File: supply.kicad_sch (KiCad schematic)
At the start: 72 parts, among them J301 Molex_Nano-Fit_1x2_SMD_105430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, Q301 DZDH0401DW, Q302 DZDH0401DW, Q303 DZDH0401DW, Q304 SQS401EN-T1_BE3, Q305 SQS401EN-T1_BE3, Q306 SQS401EN-T1_BE3, Q307 SQS401EN-T1_BE3, U301 AP62301WU-7, U302 AP62301WU-7, U303 AP62600SJ-7

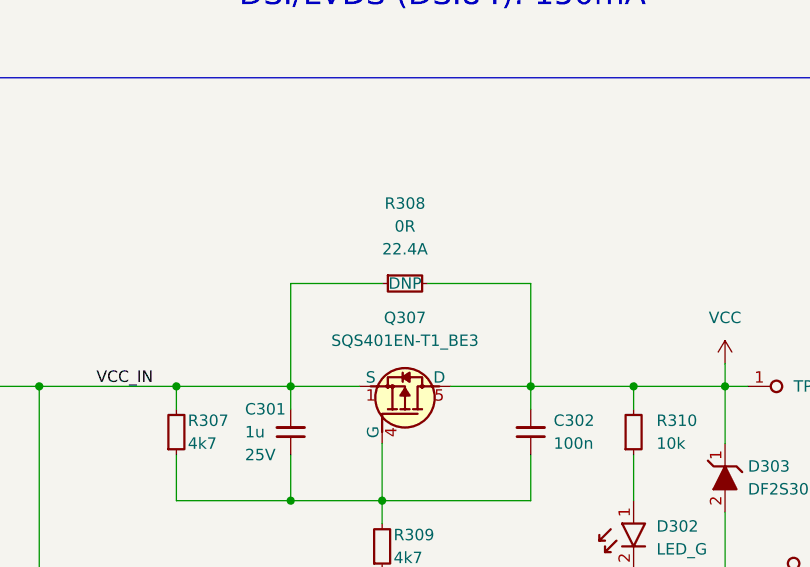
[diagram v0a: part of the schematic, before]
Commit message: Sch: Clean incorrect symbol references; Cleanup DNPs
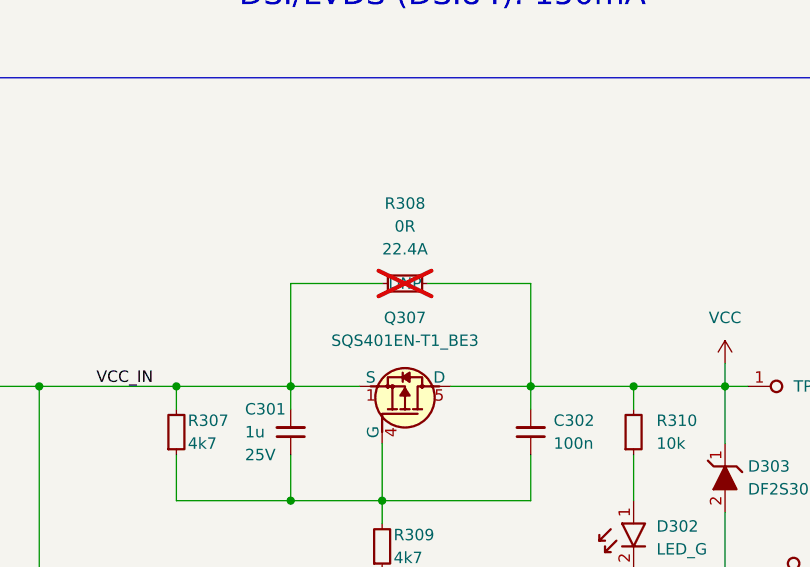
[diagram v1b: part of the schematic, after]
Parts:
- R308: now not fitted; now left out of the parts list
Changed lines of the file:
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@@
   )
   (symbol (lib_id "antmicroResistors0603:R_0R_22.4A_0603") (at 147.32 110.49 0) (unit 1)
-    (in_bom yes) (on_board yes) (dnp no)
+    (in_bom no) (on_board yes) (dnp yes)
     (property "Reference" "R308" (at 149.86 101.6 0)
       (effects (font (size 1.27 1.27)))

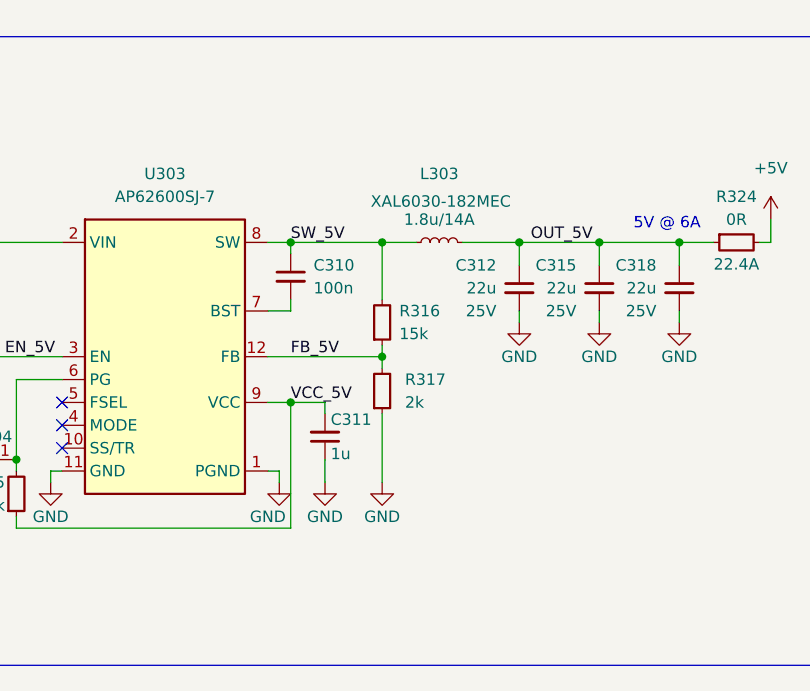
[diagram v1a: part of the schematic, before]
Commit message: [#55181] PCB: update DCDC(5V & 3V3) layout; Sch: correct 5V DCDC feedback
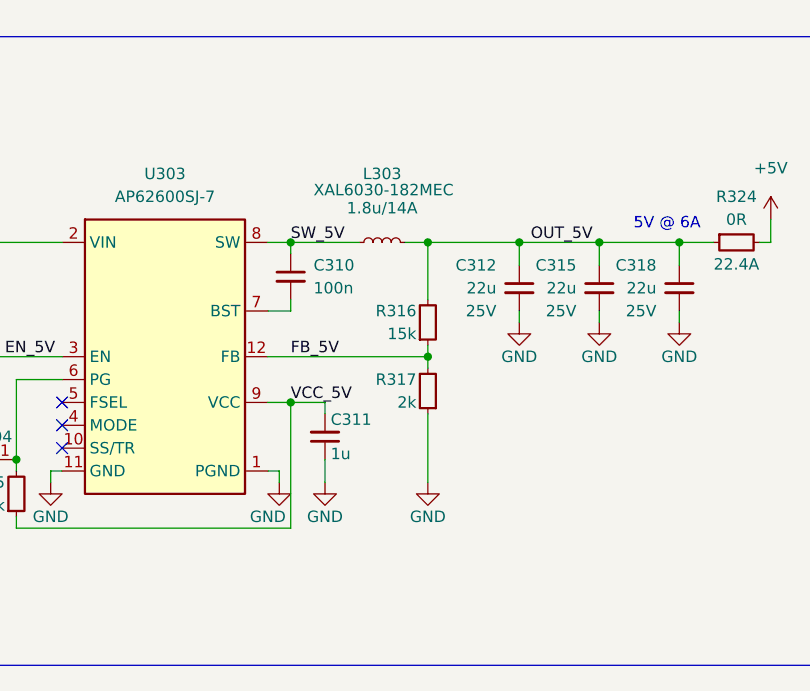
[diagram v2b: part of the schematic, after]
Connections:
- net OUT_5V: now also R316.2
- net SW_5V: no longer R316.2
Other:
- moved on the sheet: L303, R316, R317

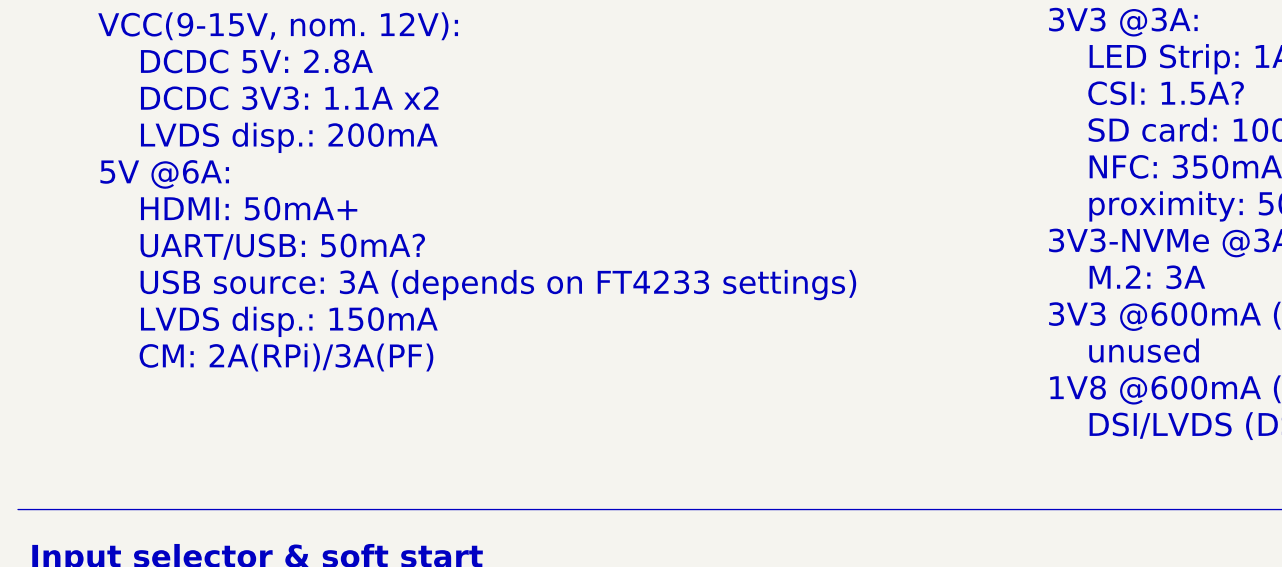
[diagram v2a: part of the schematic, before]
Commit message: [#55532] Update USB sch according to review notes; update related layout
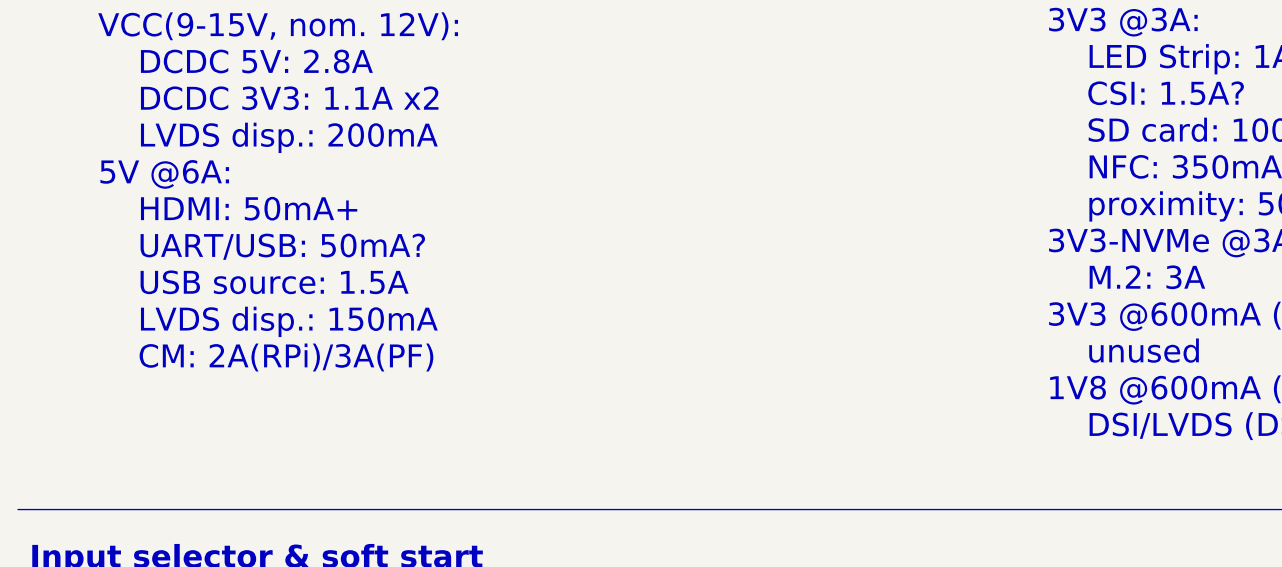
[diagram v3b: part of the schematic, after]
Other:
- note added: "VCC(9-15V, nom. 12V): DCDC 5V: 2.8A DCDC 3V3: 1.1A x2 LVDS disp.: 200mA 5V @6A: HDMI: 50mA+ UART/USB: 50mA? USB source: 1.5A LVDS disp.: 150mA CM: 2A(RPi)/3A(PF)"
- note removed: "VCC(9-15V, nom. 12V): DCDC 5V: 2.8A DCDC 3V3: 1.1A x2 LVDS disp.: 200mA 5V @6A: HDMI: 50mA+ UART/USB: 50mA? USB source: 3A (depends on FT4233 settings) LVDS disp.: 150mA CM: 2A(RPi)/3A(PF)"
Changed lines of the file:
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@@
     (effects (font (size 2.54 2.54)) (justify left bottom))
   )
-  (text "VCC(9-15V, nom. 12V):\n	DCDC 5V: 2.8A\n	DCDC 3V3: 1.1A x2\n	LVDS disp.: 200mA \n5V @6A:\n	HDMI: 50mA+\n	UART/USB: 50mA?\n	USB source: 3A (depends on FT4233 settings)\n	LVDS disp.: 150mA\n	CM: 2A(RPi)/3A(PF)\n"
+  (text "VCC(9-15V, nom. 12V):\n	DCDC 5V: 2.8A\n	DCDC 3V3: 1.1A x2\n	LVDS disp.: 200mA \n5V @6A:\n	HDMI: 50mA+\n	UART/USB: 50mA?\n	USB source: 1.5A\n	LVDS disp.: 150mA\n	CM: 2A(RPi)/3A(PF)\n"
     (at 21.59 72.39 0)
     (effects (font (size 2.54 2.54)) (justify left bottom))

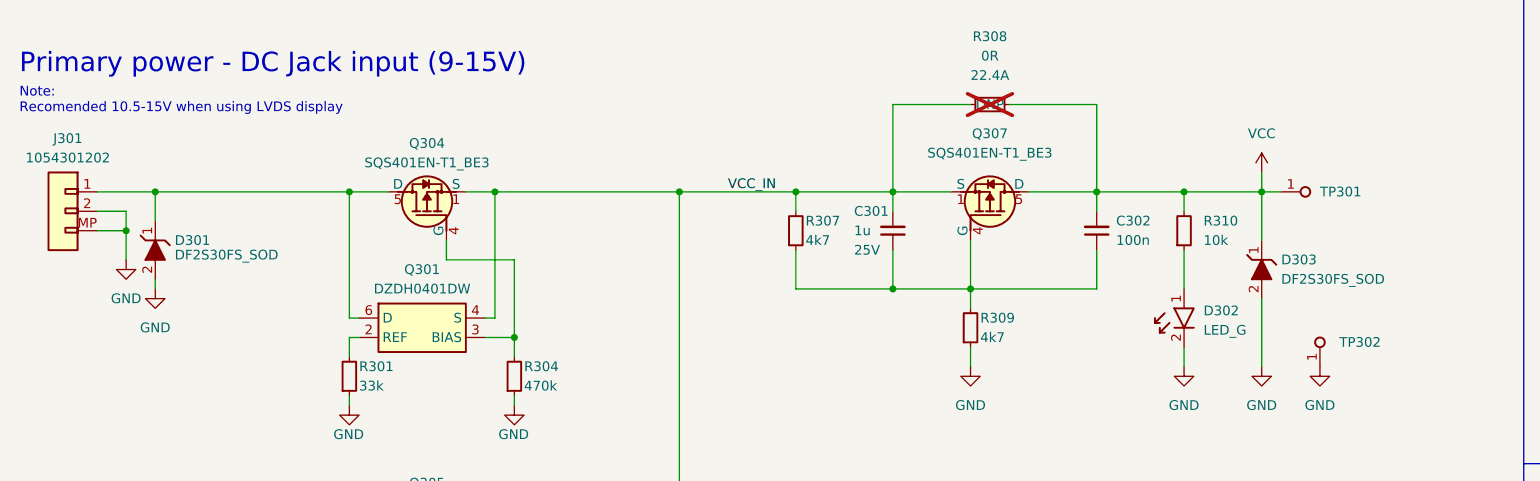
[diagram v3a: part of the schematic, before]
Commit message: [#55532] USB: add C to dcdc; add note-max Voltage; change TVS
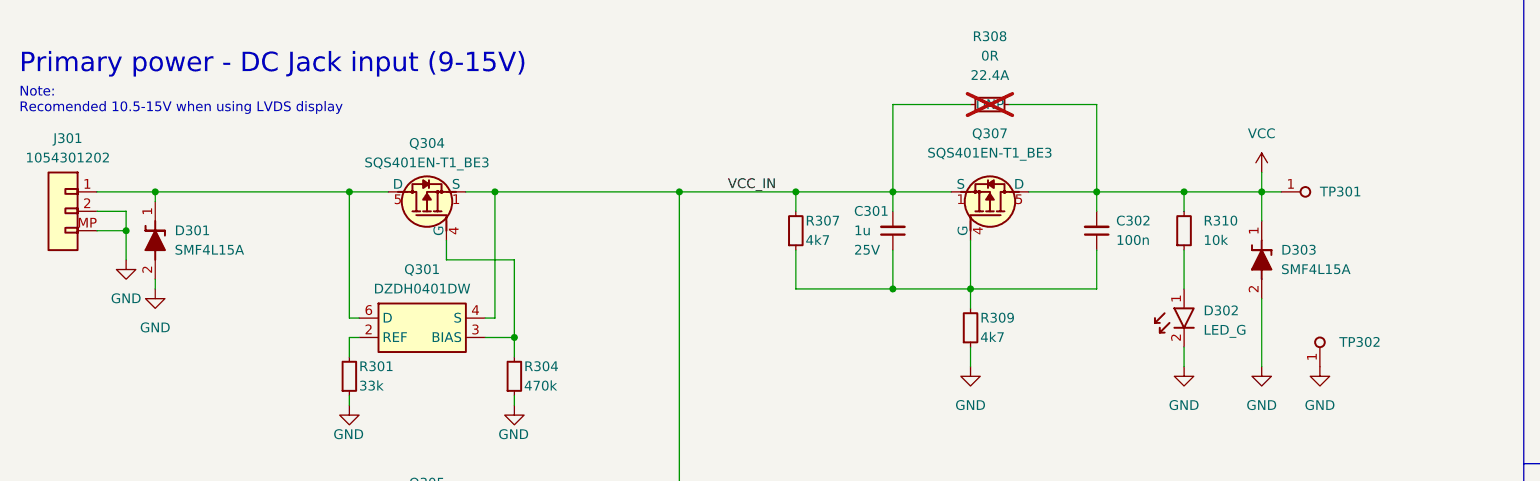
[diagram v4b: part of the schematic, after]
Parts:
- D301, D303: value DF2S30FS_SOD -> SMF4L15A; footprint antmicro-footprints:SOD-923 -> antmicro-footprints:SOD-123FL; symbol antmicroTVSDiodes:DF2S30FS_SOD -> antmicroTVSDiodes:SMF4L15A; MPN DF2S30FS -> SMF4L15A; Manufacturer Toshiba -> Infineon
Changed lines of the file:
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@@
     (stroke (width 0) (type default))
   )
+  (wire (pts (xy 40.64 121.92) (xy 66.04 121.92))
+    (stroke (width 0) (type default))
+  )
   (wire (pts (xy 363.22 113.03) (xy 363.22 110.49))
     (stroke (width 0) (type default))
@@
     (stroke (width 0) (type default))
   )
-  (wire (pts (xy 40.64 121.92) (xy 66.04 121.92))
+  (wire (pts (xy 33.02 121.92) (xy 40.64 121.92))
     (stroke (width 0) (type default))
   )
@@
     (stroke (width 0) (type default))
   )
-  (wire (pts (xy 33.02 121.92) (xy 40.64 121.92))
-    (stroke (width 0) (type default))
-  )
   (wire (pts (xy 293.37 137.16) (xy 293.37 135.89))
     (stroke (width 0) (type default))
@@
     (stroke (width 0) (type default))
   )
-  (wire (pts (xy 185.42 121.92) (xy 185.42 128.27))
+  (wire (pts (xy 185.42 121.92) (xy 185.42 125.73))
     (stroke (width 0) (type default))
   )
@@
     (stroke (width 0) (type default))
   )
-  (wire (pts (xy 40.64 121.92) (xy 40.64 125.73))
-    (stroke (width 0) (type default))
-  )
   (wire (pts (xy 289.56 231.14) (xy 290.83 231.14))
     (stroke (width 0) (type default))
@@
     (stroke (width 0) (type default))
   )
+  (wire (pts (xy 40.64 121.92) (xy 40.64 123.19))
+    (stroke (width 0) (type default))
+  )
   (wire (pts (xy 175.26 142.24) (xy 175.26 144.78))
     (stroke (width 0) (type default))
@@
     )
   )
-  (symbol (lib_id "antmicroTVSDiodes:DF2S30FS_SOD") (at 185.42 135.89 90) (unit 1)
-    (in_bom yes) (on_board yes) (dnp no)
-    (property "Reference" "D303" (at 187.96 130.81 90)
+  (symbol (lib_id "antmicroTVSDiodes:SMF4L15A") (at 185.42 135.89 90) (unit 1)
+    (in_bom yes) (on_board yes) (dnp no) (fields_autoplaced)
+    (property "Reference" "D303" (at 187.96 129.54 90)
       (effects (font (size 1.27 1.27)) (justify right))
     )
-    (property "Value" "DF2S30FS_SOD" (at 187.96 133.35 90)
-      (effects (font (size 1.27 1.27)) (justify right))
+    (property "Value" "SMF4L15A" (at 187.96 132.08 90)
+      (effects (font (size 1.27 1.27) (thickness 0.15)) (justify right))
     )
-    (property "Footprint" "antmicro-footprints:SOD-923" (at 180.34 130.81 0)
-      (effects (font (size 1.524 1.524)) (justify left bottom) hide)
+    (property "Footprint" "antmicro-footprints:SOD-123FL" (at 195.58 109.22 0)
+      (effects (font (size 1.27 1.27) (thickness 0.15)) (justify left bottom) hide)
     )
-    (property "Datasheet" "https://www.mouser.com/datasheet/2/408/DF2S30FS_datasheet_en_20211216-1916197.pdf" (at 177.8 130.81 0)
-      (effects (font (size 1.524 1.524)) (justify left bottom) hide)
+    (property "Datasheet" "https://www.mouser.com/datasheet/2/240/Littelfuse_TVS_Diode_SMF4L_Datasheet_pdf-1665786.pdf" (at 198.12 109.22 0)
+      (effects (font (size 1.27 1.27) (thickness 0.15)) (justify left bottom) hide)
     )
-    (property "Manufacturer" "Toshiba" (at 157.48 130.81 0)
-      (effects (font (size 1.524 1.524)) (justify left bottom) hide)
+    (property "Manufacturer" "Infineon" (at 203.2 109.22 0)
+      (effects (font (size 1.27 1.27) (thickness 0.15)) (justify left bottom) hide)
     )
-    (property "MPN" "DF2S30FS" (at 172.72 130.81 0)
-      (effects (font (size 1.524 1.524)) (justify left bottom) hide)
+    (property "MPN" "SMF4L15A" (at 200.66 109.22 0)
+      (effects (font (size 1.27 1.27) (thickness 0.15)) (justify left bottom) hide)
     )
-    (property "Author" "Antmicro" (at 203.2 114.3 0)
+    (property "Author" "Antmicro" (at 205.74 109.22 0)
       (effects (font (size 1.27 1.27) (thickness 0.15)) (justify left bottom) hide)
     )
-    (property "License" "Apache-2.0" (at 205.74 114.3 0)
+    (property "License" "Apache-2.0" (at 208.28 109.22 0)
       (effects (font (size 1.27 1.27) (thickness 0.15)) (justify left bottom) hide)
     )
@@
     )
   )
-  (symbol (lib_id "antmicroTVSDiodes:DF2S30FS_SOD") (at 40.64 133.35 90) (unit 1)
-    (in_bom yes) (on_board yes) (dnp no)
-    (property "Reference" "D301" (at 43.18 128.27 90)
+  (symbol (lib_id "antmicroTVSDiodes:SMF4L15A") (at 40.64 133.35 90) (unit 1)
+    (in_bom yes) (on_board yes) (dnp no) (fields_autoplaced)
+    (property "Reference" "D301" (at 43.18 127 90)
       (effects (font (size 1.27 1.27)) (justify right))
     )
-    (property "Value" "DF2S30FS_SOD" (at 43.18 130.175 90)
-      (effects (font (size 1.27 1.27)) (justify right))
+    (property "Value" "SMF4L15A" (at 43.18 129.54 90)
+      (effects (font (size 1.27 1.27) (thickness 0.15)) (justify right))
     )
-    (property "Footprint" "antmicro-footprints:SOD-923" (at 35.56 128.27 0)
-      (effects (font (size 1.524 1.524)) (justify left bottom) hide)
+    (property "Footprint" "antmicro-footprints:SOD-123FL" (at 50.8 106.68 0)
+      (effects (font (size 1.27 1.27) (thickness 0.15)) (justify left bottom) hide)
     )
-    (property "Datasheet" "https://www.mouser.com/datasheet/2/408/DF2S30FS_datasheet_en_20211216-1916197.pdf" (at 33.02 128.27 0)
-      (effects (font (size 1.524 1.524)) (justify left bottom) hide)
+    (property "Datasheet" "https://www.mouser.com/datasheet/2/240/Littelfuse_TVS_Diode_SMF4L_Datasheet_pdf-1665786.pdf" (at 53.34 106.68 0)
+      (effects (font (size 1.27 1.27) (thickness 0.15)) (justify left bottom) hide)
     )
-    (property "Manufacturer" "Toshiba" (at 12.7 128.27 0)
-      (effects (font (size 1.524 1.524)) (justify left bottom) hide)
+    (property "Manufacturer" "Infineon" (at 58.42 106.68 0)
+      (effects (font (size 1.27 1.27) (thickness 0.15)) (justify left bottom) hide)
     )
-    (property "MPN" "DF2S30FS" (at 27.94 128.27 0)
-      (effects (font (size 1.524 1.524)) (justify left bottom) hide)
+    (property "MPN" "SMF4L15A" (at 55.88 106.68 0)
+      (effects (font (size 1.27 1.27) (thickness 0.15)) (justify left bottom) hide)
     )
-    (property "Author" "Antmicro" (at 58.42 111.76 0)
+    (property "Author" "Antmicro" (at 60.96 106.68 0)
       (effects (font (size 1.27 1.27) (thickness 0.15)) (justify left bottom) hide)
     )
-    (property "License" "Apache-2.0" (at 60.96 111.76 0)
+    (property "License" "Apache-2.0" (at 63.5 106.68 0)
       (effects (font (size 1.27 1.27) (thickness 0.15)) (justify left bottom) hide)
     )
